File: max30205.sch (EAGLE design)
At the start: 7 parts, among them J5 DNP, J6 DNP, U1 MAX30205MTA+T21-0137I_T833-2_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

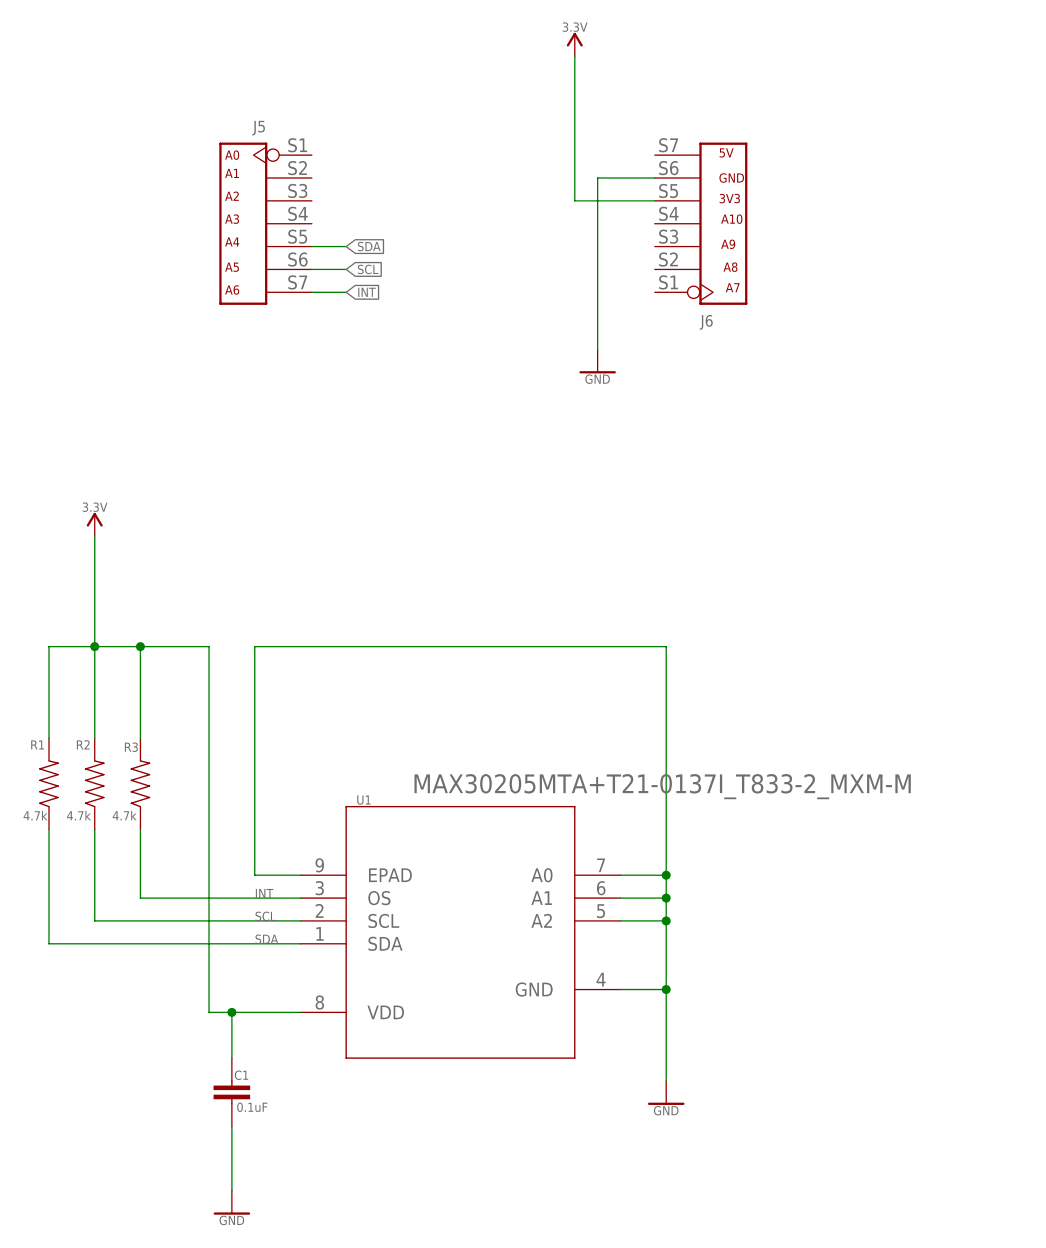
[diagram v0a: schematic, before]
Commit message: Update max30205.sch
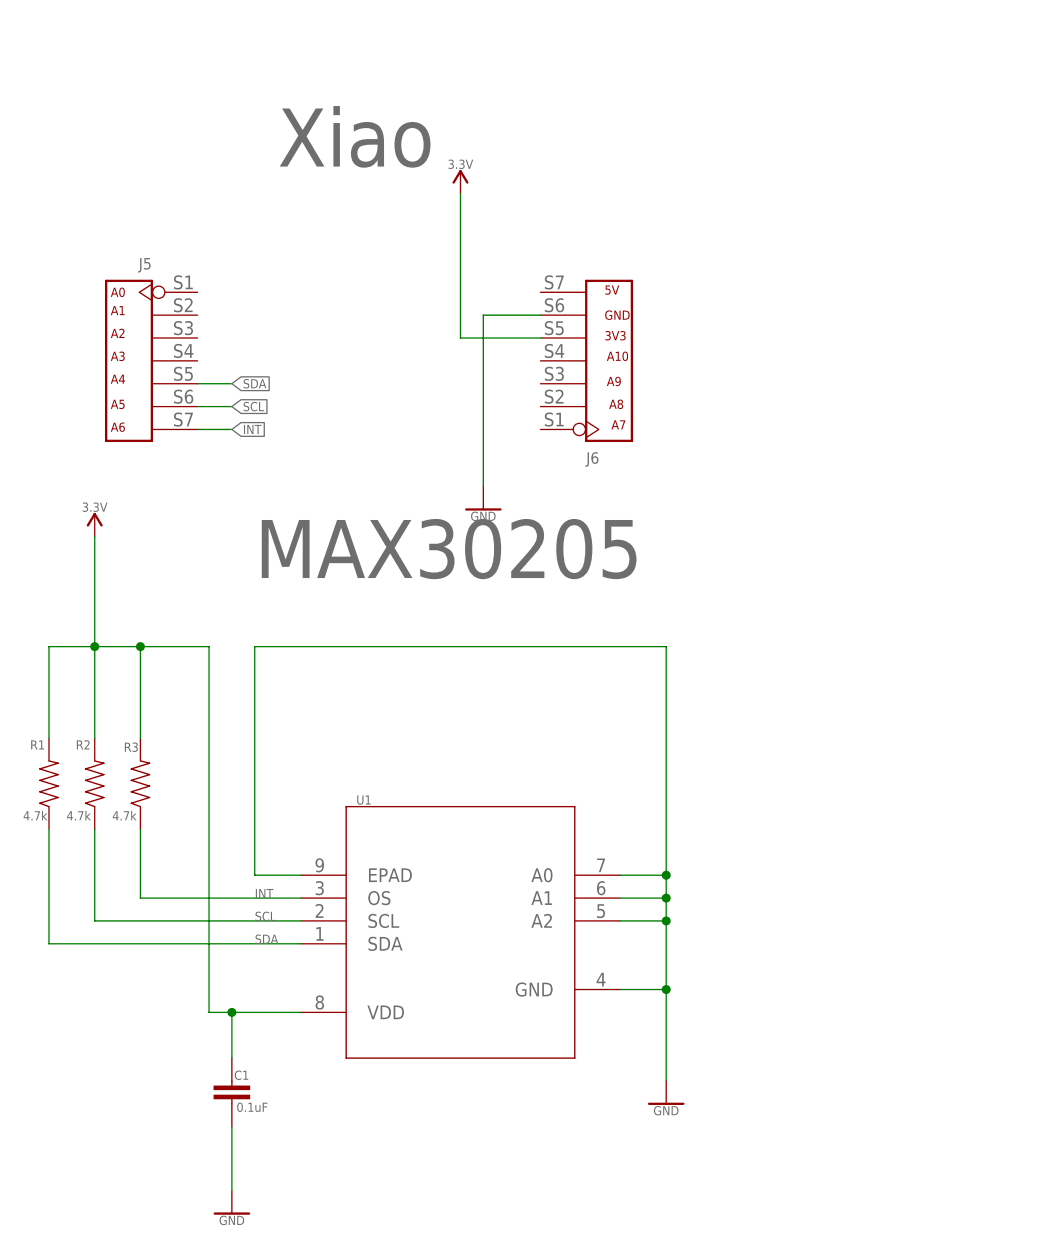
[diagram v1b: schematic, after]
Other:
- note added: "MAX30205"
- note added: "Xiao"
- moved on the sheet: J5, J6
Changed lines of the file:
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@@
 <?xml version="1.0" encoding="utf-8"?>
 <!DOCTYPE eagle SYSTEM "eagle.dtd">
-<eagle version="9.5.0">
+<eagle version="9.6.0">
 <drawing>
 <settings>
@@
 <sheet>
 <plain>
-<text x="37.338" y="158.242" size="1.016" layer="94" font="vector" ratio="20">A0</text>
-<text x="37.338" y="156.21" size="1.016" layer="94" font="vector" ratio="20">A1</text>
-<text x="37.338" y="153.67" size="1.016" layer="94" font="vector" ratio="20">A2</text>
-<text x="37.338" y="151.13" size="1.016" layer="94" font="vector" ratio="20">A3</text>
-<text x="37.338" y="148.59" size="1.016" layer="94" font="vector" ratio="20">A4</text>
-<text x="37.338" y="145.796" size="1.016" layer="94" font="vector" ratio="20">A5</text>
-<text x="37.338" y="143.256" size="1.016" layer="94" font="vector" ratio="20">A6</text>
-<text x="92.964" y="143.51" size="1.016" layer="94" font="vector" ratio="20">A7</text>
-<text x="92.71" y="145.796" size="1.016" layer="94" font="vector" ratio="20">A8</text>
-<text x="92.456" y="148.336" size="1.016" layer="94" font="vector" ratio="20">A9</text>
-<text x="92.456" y="151.13" size="1.016" layer="94" font="vector" ratio="20">A10</text>
-<text x="92.202" y="158.496" size="1.016" layer="94" font="vector" ratio="20">5V</text>
-<text x="92.202" y="153.416" size="1.016" layer="94" font="vector" ratio="20">3V3</text>
-<text x="92.202" y="155.702" size="1.016" layer="94" font="vector" ratio="20">GND</text>
+<text x="24.638" y="143.002" size="1.016" layer="94" font="vector" ratio="20">A0</text>
+<text x="24.638" y="140.97" size="1.016" layer="94" font="vector" ratio="20">A1</text>
+<text x="24.638" y="138.43" size="1.016" layer="94" font="vector" ratio="20">A2</text>
+<text x="24.638" y="135.89" size="1.016" layer="94" font="vector" ratio="20">A3</text>
+<text x="24.638" y="133.35" size="1.016" layer="94" font="vector" ratio="20">A4</text>
+<text x="24.638" y="130.556" size="1.016" layer="94" font="vector" ratio="20">A5</text>
+<text x="24.638" y="128.016" size="1.016" layer="94" font="vector" ratio="20">A6</text>
+<text x="80.264" y="128.27" size="1.016" layer="94" font="vector" ratio="20">A7</text>
+<text x="80.01" y="130.556" size="1.016" layer="94" font="vector" ratio="20">A8</text>
+<text x="79.756" y="133.096" size="1.016" layer="94" font="vector" ratio="20">A9</text>
+<text x="79.756" y="135.89" size="1.016" layer="94" font="vector" ratio="20">A10</text>
+<text x="79.502" y="143.256" size="1.016" layer="94" font="vector" ratio="20">5V</text>
+<text x="79.502" y="138.176" size="1.016" layer="94" font="vector" ratio="20">3V3</text>
+<text x="79.502" y="140.462" size="1.016" layer="94" font="vector" ratio="20">GND</text>
+<text x="43.18" y="157.48" size="6.4516" layer="95" font="vector" ratio="20">Xiao</text>
+<text x="40.64" y="111.76" size="6.4516" layer="95" font="vector" ratio="20">MAX30205</text>
 </plain>
 <instances>
-<instance part="J5" gate="G$1" x="39.37" y="151.13" smashed="yes" rot="MR0">
-<attribute name="NAME" x="41.91" y="161.29" size="1.27" layer="95" ratio="12" rot="MR0"/>
-</instance>
-<instance part="J6" gate="G$1" x="92.71" y="151.13" smashed="yes" rot="MR180">
-<attribute name="NAME" x="90.17" y="140.97" size="1.27" layer="95" ratio="12" rot="MR180"/>
+<instance part="J5" gate="G$1" x="26.67" y="135.89" smashed="yes" rot="MR0">
+<attribute name="NAME" x="29.21" y="146.05" size="1.27" layer="95" ratio="12" rot="MR0"/>
+</instance>
+<instance part="J6" gate="G$1" x="80.01" y="135.89" smashed="yes" rot="MR180">
+<attribute name="NAME" x="77.47" y="125.73" size="1.27" layer="95" ratio="12" rot="MR180"/>
 </instance>
 <instance part="FRAME3" gate="G$1" x="0" y="0" smashed="yes">
@@
 <attribute name="SHEET" x="230.505" y="5.08" size="2.54" layer="94"/>
 </instance>
-<instance part="GND3" gate="1" x="78.74" y="134.62" smashed="yes">
-<attribute name="VALUE" x="78.74" y="134.366" size="1.016" layer="96" font="vector" ratio="20" align="top-center"/>
+<instance part="GND3" gate="1" x="66.04" y="119.38" smashed="yes">
+<attribute name="VALUE" x="66.04" y="119.126" size="1.016" layer="96" font="vector" ratio="20" align="top-center"/>
 </instance>
 <instance part="U1" gate="A" x="43.18" y="78.74" smashed="yes">
 <attribute name="NAME" x="51.9176" y="86.5886" size="1.016" layer="95" font="vector" ratio="20" rot="SR0"/>
-<attribute name="VALUE" x="58.1406" y="87.8586" size="2.0828" layer="96" ratio="6" rot="SR0"/>
+<attribute name="VALUE" x="58.1406" y="87.8586" size="2.0828" layer="96" ratio="6" rot="SR0" display="off"/>
 </instance>
 <instance part="GND1" gate="1" x="86.36" y="53.34" smashed="yes">
 <attribute name="VALUE" x="86.36" y="53.086" size="1.016" layer="96" font="vector" ratio="20" align="top-center"/>
 </instance>
-<instance part="SUPPLY1" gate="G$1" x="76.2" y="169.672" smashed="yes">
-<attribute name="VALUE" x="76.2" y="172.466" size="1.016" layer="96" font="vector" ratio="20" align="bottom-center"/>
+<instance part="SUPPLY1" gate="G$1" x="63.5" y="154.432" smashed="yes">
+<attribute name="VALUE" x="63.5" y="157.226" size="1.016" layer="96" font="vector" ratio="20" align="bottom-center"/>
 </instance>
 <instance part="R1" gate="G$1" x="17.78" y="88.9" smashed="yes" rot="R90">
@@
 <pinref part="J6" gate="G$1" pin="6"/>
 <pinref part="GND3" gate="1" pin="GND"/>
-<wire x1="85.09" y1="156.21" x2="78.74" y2="156.21" width="0.1524" layer="91"/>
-<wire x1="78.74" y1="156.21" x2="78.74" y2="137.16" width="0.1524" layer="91"/>
+<wire x1="72.39" y1="140.97" x2="66.04" y2="140.97" width="0.1524" layer="91"/>
+<wire x1="66.04" y1="140.97" x2="66.04" y2="121.92" width="0.1524" layer="91"/>
 </segment>
 <segment>
@@
 <segment>
 <pinref part="J5" gate="G$1" pin="5"/>
-<wire x1="46.99" y1="148.59" x2="50.8" y2="148.59" width="0.1524" layer="91"/>
-<label x="50.8" y="148.59" size="1.016" layer="95" font="vector" ratio="20" xref="yes"/>
+<wire x1="34.29" y1="133.35" x2="38.1" y2="133.35" width="0.1524" layer="91"/>
+<label x="38.1" y="133.35" size="1.016" layer="95" font="vector" ratio="20" xref="yes"/>
 </segment>
 <segment>
@@
 <segment>
 <pinref part="J5" gate="G$1" pin="6"/>
-<wire x1="46.99" y1="146.05" x2="50.8" y2="146.05" width="0.1524" layer="91"/>
-<label x="50.8" y="146.05" size="1.016" layer="95" font="vector" ratio="20" xref="yes"/>
+<wire x1="34.29" y1="130.81" x2="38.1" y2="130.81" width="0.1524" layer="91"/>
+<label x="38.1" y="130.81" size="1.016" layer="95" font="vector" ratio="20" xref="yes"/>
 </segment>
 <segment>
@@
 <segment>
 <pinref part="J5" gate="G$1" pin="7"/>
-<wire x1="46.99" y1="143.51" x2="50.8" y2="143.51" width="0.1524" layer="91"/>
-<label x="50.8" y="143.51" size="1.016" layer="95" font="vector" ratio="20" xref="yes"/>
+<wire x1="34.29" y1="128.27" x2="38.1" y2="128.27" width="0.1524" layer="91"/>
+<label x="38.1" y="128.27" size="1.016" layer="95" font="vector" ratio="20" xref="yes"/>
 </segment>
 <segment>
@@
 <segment>
 <pinref part="J6" gate="G$1" pin="5"/>
-<wire x1="85.09" y1="153.67" x2="76.2" y2="153.67" width="0.1524" layer="91"/>
-<wire x1="76.2" y1="153.67" x2="76.2" y2="169.672" width="0.1524" layer="91"/>
+<wire x1="72.39" y1="138.43" x2="63.5" y2="138.43" width="0.1524" layer="91"/>
+<wire x1="63.5" y1="138.43" x2="63.5" y2="154.432" width="0.1524" layer="91"/>
 <pinref part="SUPPLY1" gate="G$1" pin="3.3V"/>
 </segment>
